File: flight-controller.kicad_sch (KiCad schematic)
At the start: 50 parts, among them J1 USB_C_Receptacle_USB2.0_16P, J2 Conn_Coaxial, J4 TC2030, SW1 SW_Push, U1 MIC5365-3.3YD5, U2 USBLC6-2SC6, U3 DLF162500LT-5028A1, U4 STM32WB55CEUx, U5 MPU-6050, X1 32kHz768, X2 32MHz

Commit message: BOM updates, minor routing improvements
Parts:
- C1, C14, C2, C3, C6: Distributor Link https://www.mouser.com/ProductDetail/KYOCERA-AVX/0603ZD475M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 -> https://www.digikey.com/en/products/detail/kyocera-avx/0402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
- C10, C11, C12, C13, C19, C20, C22, C4, C5, C7, C8, C9: Distributor Link https://www.mouser.com/ProductDetail/KYOCERA-AVX/0402X7R104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 -> https://www.digikey.com/en/products/detail/kyocera-avx/KGM0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; Manufacturer Part # 0402X7R104KT7AT -> KGM05AR51A104KH
- C15: Distributor Link (none) -> https://www.digikey.com/en/products/detail/kyocera-avx/0402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; Manufacturer (none) -> Kyocera AVX; Manufacturer Part # (none) -> 04025U0R8BAT2A
- C17, C18: Manufacturer (none) -> NOTE: Should make of type C0G
- X2: Distributor Link (none) -> https://www.digikey.com/en/products/detail/ndk-america-inc/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
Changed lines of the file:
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@@
 			)
 		)
-		(property "Distributor Link" "https://www.mouser.com/ProductDetail/KYOCERA-AVX/0402X7R104KT7AT?qs=sGAEpiMZZMukHu%252BjC5l7YTEDUe5eStCUp1B9Y37Xni8%3D"
+		(property "Distributor Link" "https://www.digikey.com/en/products/detail/kyocera-avx/KGM05AR51A104KH/563239"
 			(at 92.71 43.18 0)
 			(effects
@@
 			)
 		)
-		(property "Manufacturer Part #" "0402X7R104KT7AT"
+		(property "Manufacturer Part #" "KGM05AR51A104KH"
 			(at 92.71 43.18 0)
 			(effects
@@
 			)
 		)
-		(property "Manufacturer" ""
+		(property "Manufacturer" "NOTE: Should make of type C0G"
 			(at 166.37 110.49 0)
 			(effects
@@
 			)
 		)
-		(property "Distributor Link" "https://www.mouser.com/ProductDetail/KYOCERA-AVX/0402X7R104KT7AT?qs=sGAEpiMZZMukHu%252BjC5l7YTEDUe5eStCUp1B9Y37Xni8%3D"
+		(property "Distributor Link" "https://www.digikey.com/en/products/detail/kyocera-avx/KGM05AR51A104KH/563239"
 			(at 101.6 170.18 0)
 			(effects
@@
 			)
 		)
-		(property "Manufacturer Part #" "0402X7R104KT7AT"
+		(property "Manufacturer Part #" "KGM05AR51A104KH"
 			(at 101.6 170.18 0)
 			(effects
@@
 			)
 		)
-		(property "Distributor Link" "https://www.mouser.com/ProductDetail/KYOCERA-AVX/0603ZD475MAT2A?qs=sGAEpiMZZMsh%252B1woXyUXj3kzDK1MKLImRlrG%252BuVm%252Bt8%3D"
+		(property "Distributor Link" "https://www.digikey.com/en/products/detail/kyocera-avx/0402ZD475MAT2A/3080850"
 			(at 41.91 43.18 0)
 			(effects
@@
 			)
 		)
-		(property "Distributor Link" ""
+		(property "Distributor Link" "https://www.digikey.com/en/products/detail/kyocera-avx/04025U0R8BAT2A/2136276"
 			(at 201.93 86.36 0)
 			(effects
@@
 			)
 		)
-		(property "Manufacturer" ""
+		(property "Manufacturer" "Kyocera AVX"
 			(at 201.93 86.36 0)
 			(effects
@@
 			)
 		)
-		(property "Manufacturer Part #" ""
+		(property "Manufacturer Part #" "04025U0R8BAT2A"
 			(at 201.93 86.36 0)
 			(effects
@@
 			)
 		)
-		(property "Distributor Link" "https://www.mouser.com/ProductDetail/KYOCERA-AVX/0402X7R104KT7AT?qs=sGAEpiMZZMukHu%252BjC5l7YTEDUe5eStCUp1B9Y37Xni8%3D"
+		(property "Distributor Link" "https://www.digikey.com/en/products/detail/kyocera-avx/KGM05AR51A104KH/563239"
 			(at 139.7 27.94 0)
 			(effects
@@
 			)
 		)
-		(property "Manufacturer Part #" "0402X7R104KT7AT"
+		(property "Manufacturer Part #" "KGM05AR51A104KH"
 			(at 139.7 27.94 0)
 			(effects
@@
 			)
 		)
-		(property "Distributor Link" "https://www.mouser.com/ProductDetail/KYOCERA-AVX/0603ZD475MAT2A?qs=sGAEpiMZZMsh%252B1woXyUXj3kzDK1MKLImRlrG%252BuVm%252Bt8%3D"
+		(property "Distributor Link" "https://www.digikey.com/en/products/detail/kyocera-avx/0402ZD475MAT2A/3080850"
 			(at 87.63 26.67 0)
 			(effects
@@
 			)
 		)
-		(property "Distributor Link" "https://www.mouser.com/ProductDetail/KYOCERA-AVX/0603ZD475MAT2A?qs=sGAEpiMZZMsh%252B1woXyUXj3kzDK1MKLImRlrG%252BuVm%252Bt8%3D"
+		(property "Distributor Link" "https://www.digikey.com/en/products/detail/kyocera-avx/0402ZD475MAT2A/3080850"
 			(at 49.53 25.4 0)
 			(effects
@@
 			)
 		)
-		(property "Distributor Link" "https://www.mouser.com/ProductDetail/KYOCERA-AVX/0402X7R104KT7AT?qs=sGAEpiMZZMukHu%252BjC5l7YTEDUe5eStCUp1B9Y37Xni8%3D"
+		(property "Distributor Link" "https://www.digikey.com/en/products/detail/kyocera-avx/KGM05AR51A104KH/563239"
 			(at 105.41 43.18 0)
 			(effects
@@
 			)
 		)
-		(property "Manufacturer Part #" "0402X7R104KT7AT"
+		(property "Manufacturer Part #" "KGM05AR51A104KH"
 			(at 105.41 43.18 0)
 			(effects
@@
 			)
 		)
-		(property "Distributor Link" "https://www.mouser.com/ProductDetail/KYOCERA-AVX/0402X7R104KT7AT?qs=sGAEpiMZZMukHu%252BjC5l7YTEDUe5eStCUp1B9Y37Xni8%3D"
+		(property "Distributor Link" "https://www.digikey.com/en/products/detail/kyocera-avx/KGM05AR51A104KH/563239"
 			(at 121.92 26.67 0)
 			(effects
@@
 			)
 		)
-		(property "Manufacturer Part #" "0402X7R104KT7AT"
+		(property "Manufacturer Part #" "KGM05AR51A104KH"
 			(at 121.92 26.67 0)
 			(effects
@@
 			)
 		)
-		(property "Distributor Link" "https://www.mouser.com/ProductDetail/KYOCERA-AVX/0402X7R104KT7AT?qs=sGAEpiMZZMukHu%252BjC5l7YTEDUe5eStCUp1B9Y37Xni8%3D"
+		(property "Distributor Link" "https://www.digikey.com/en/products/detail/kyocera-avx/KGM05AR51A104KH/563239"
 			(at 210.82 115.57 0)
 			(effects
@@
 			)
 		)
-		(property "Manufacturer Part #" "0402X7R104KT7AT"
+		(property "Manufacturer Part #" "KGM05AR51A104KH"
 			(at 210.82 115.57 0)
 			(effects
@@
 			)
 		)
-		(property "Distributor Link" "https://www.mouser.com/ProductDetail/KYOCERA-AVX/0402X7R104KT7AT?qs=sGAEpiMZZMukHu%252BjC5l7YTEDUe5eStCUp1B9Y37Xni8%3D"
+		(property "Distributor Link" "https://www.digikey.com/en/products/detail/kyocera-avx/KGM05AR51A104KH/563239"
 			(at 80.01 43.18 0)
 			(effects
@@
 			)
 		)
-		(property "Manufacturer Part #" "0402X7R104KT7AT"
+		(property "Manufacturer Part #" "KGM05AR51A104KH"
 			(at 80.01 43.18 0)
 			(effects
@@
 			)
 		)
-		(property "Distributor Link" "https://www.mouser.com/ProductDetail/KYOCERA-AVX/0603ZD475MAT2A?qs=sGAEpiMZZMsh%252B1woXyUXj3kzDK1MKLImRlrG%252BuVm%252Bt8%3D"
+		(property "Distributor Link" "https://www.digikey.com/en/products/detail/kyocera-avx/0402ZD475MAT2A/3080850"
 			(at 109.22 26.67 0)
 			(effects
@@
 			)
 		)
-		(property "Distributor Link" "https://www.mouser.com/ProductDetail/KYOCERA-AVX/0402X7R104KT7AT?qs=sGAEpiMZZMukHu%252BjC5l7YTEDUe5eStCUp1B9Y37Xni8%3D"
+		(property "Distributor Link" "https://www.digikey.com/en/products/detail/kyocera-avx/KGM05AR51A104KH/563239"
 			(at 190.5 49.53 0)
 			(effects
@@
 			)
 		)
-		(property "Manufacturer Part #" "0402X7R104KT7AT"
+		(property "Manufacturer Part #" "KGM05AR51A104KH"
 			(at 190.5 49.53 0)
 			(effects
@@
 			)
 		)
-		(property "Distributor Link" ""
+		(property "Distributor Link" "https://www.digikey.com/en/products/detail/ndk-america-inc/CS06465-32M/7645290"
 			(at 193.04 100.33 0)
 			(effects
@@
 			)
 		)
-		(property "Distributor Link" "https://www.mouser.com/ProductDetail/KYOCERA-AVX/0402X7R104KT7AT?qs=sGAEpiMZZMukHu%252BjC5l7YTEDUe5eStCUp1B9Y37Xni8%3D"
+		(property "Distributor Link" "https://www.digikey.com/en/products/detail/kyocera-avx/KGM05AR51A104KH/563239"
 			(at 54.61 43.18 0)
 			(effects
@@
 			)
 		)
-		(property "Manufacturer Part #" "0402X7R104KT7AT"
+		(property "Manufacturer Part #" "KGM05AR51A104KH"
 			(at 54.61 43.18 0)
 			(effects
@@
 			)
 		)
-		(property "Distributor Link" "https://www.mouser.com/ProductDetail/KYOCERA-AVX/0402X7R104KT7AT?qs=sGAEpiMZZMukHu%252BjC5l7YTEDUe5eStCUp1B9Y37Xni8%3D"
+		(property "Distributor Link" "https://www.digikey.com/en/products/detail/kyocera-avx/KGM05AR51A104KH/563239"
 			(at 118.11 43.18 0)
 			(effects
@@
 			)
 		)
-		(property "Manufacturer Part #" "0402X7R104KT7AT"
+		(property "Manufacturer Part #" "KGM05AR51A104KH"
 			(at 118.11 43.18 0)
 			(effects
@@
 			)
 		)
-		(property "Distributor Link" "https://www.mouser.com/ProductDetail/KYOCERA-AVX/0402X7R104KT7AT?qs=sGAEpiMZZMukHu%252BjC5l7YTEDUe5eStCUp1B9Y37Xni8%3D"
+		(property "Distributor Link" "https://www.digikey.com/en/products/detail/kyocera-avx/KGM05AR51A104KH/563239"
 			(at 64.77 184.15 0)
 			(effects
@@
 			)
 		)
-		(property "Manufacturer Part #" "0402X7R104KT7AT"
+		(property "Manufacturer Part #" "KGM05AR51A104KH"
 			(at 64.77 184.15 0)
 			(effects
@@
 			)
 		)
-		(property "Manufacturer" ""
+		(property "Manufacturer" "NOTE: Should make of type C0G"
 			(at 176.53 110.49 0)
 			(effects
@@
 			)
 		)
-		(property "Distributor Link" "https://www.mouser.com/ProductDetail/KYOCERA-AVX/0402X7R104KT7AT?qs=sGAEpiMZZMukHu%252BjC5l7YTEDUe5eStCUp1B9Y37Xni8%3D"
+		(property "Distributor Link" "https://www.digikey.com/en/products/detail/kyocera-avx/KGM05AR51A104KH/563239"
 			(at 67.31 43.18 0)
 			(effects
@@
 			)
 		)
-		(property "Manufacturer Part #" "0402X7R104KT7AT"
+		(property "Manufacturer Part #" "KGM05AR51A104KH"
 			(at 67.31 43.18 0)
 			(effects
@@
 			)
 		)
-		(property "Distributor Link" "https://www.mouser.com/ProductDetail/KYOCERA-AVX/0603ZD475MAT2A?qs=sGAEpiMZZMsh%252B1woXyUXj3kzDK1MKLImRlrG%252BuVm%252Bt8%3D"
+		(property "Distributor Link" "https://www.digikey.com/en/products/detail/kyocera-avx/0402ZD475MAT2A/3080850"
 			(at 190.5 66.04 0)
 			(effects

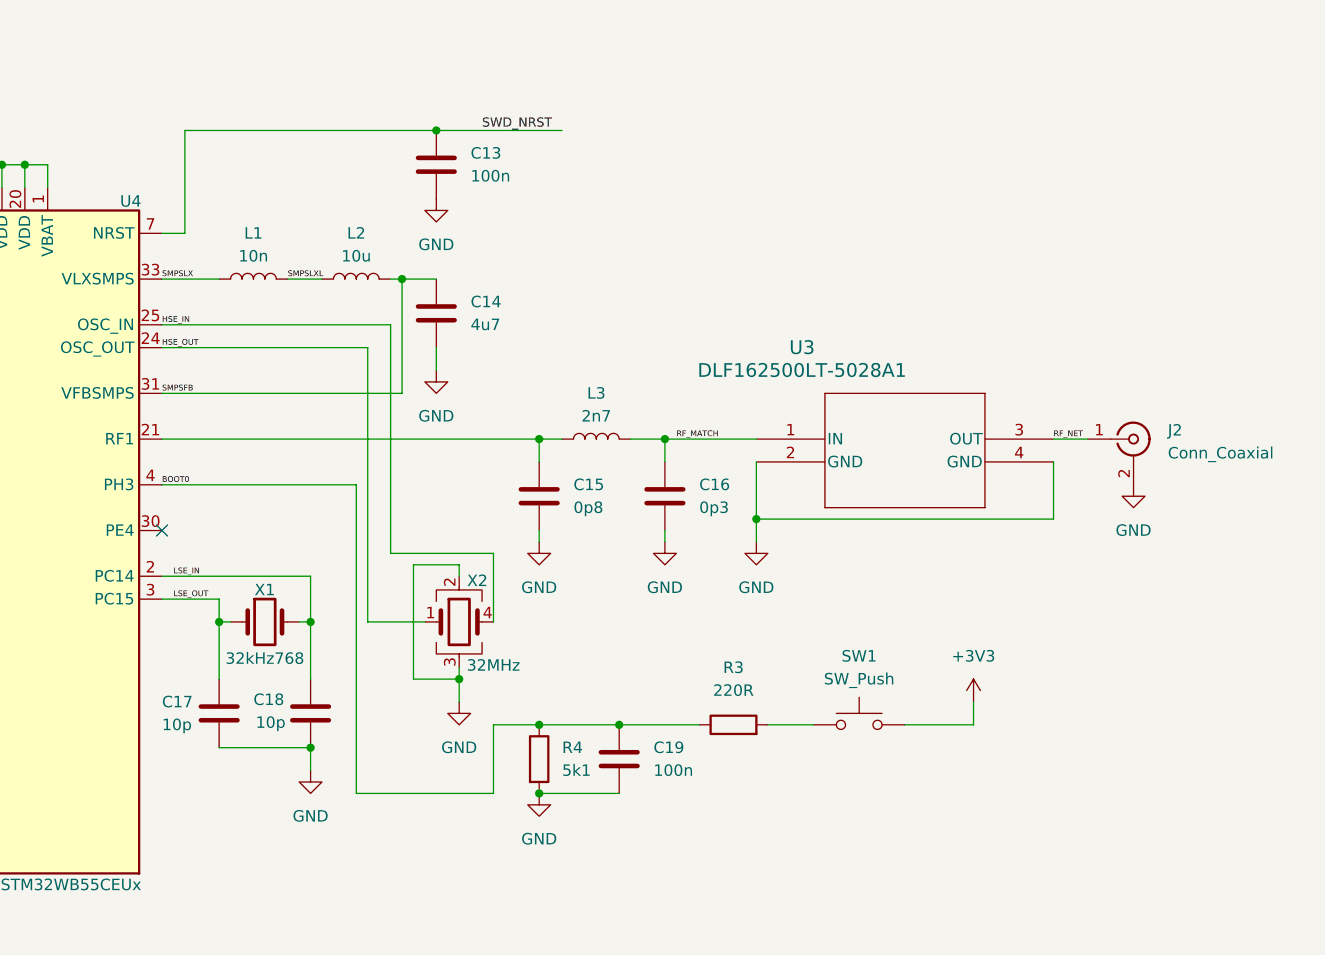
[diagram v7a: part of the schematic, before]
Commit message: BOM done, footprints & layout updated.
Layout for both crystal oscillators revised.
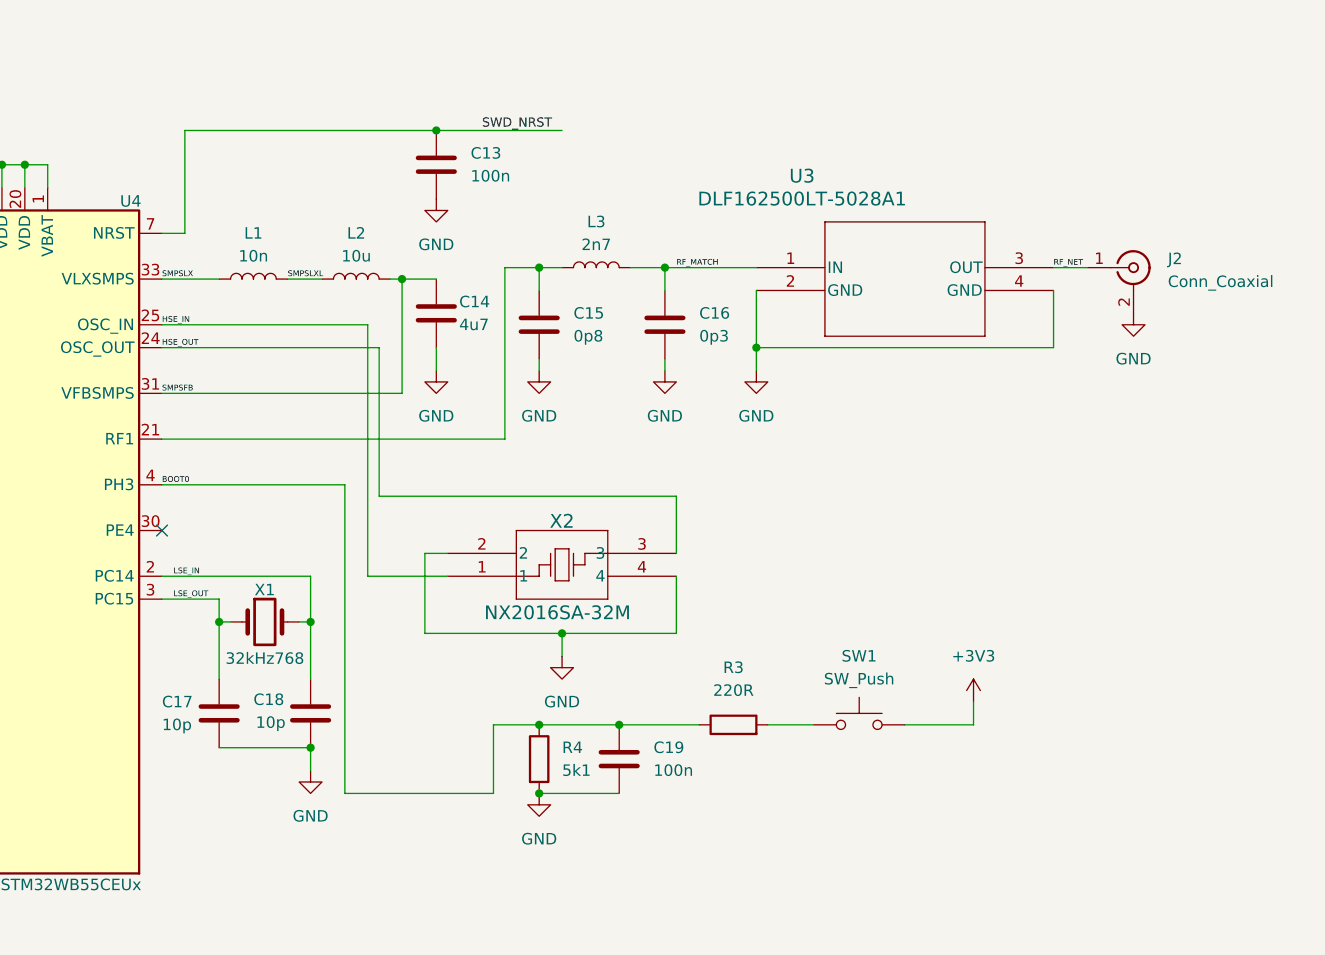
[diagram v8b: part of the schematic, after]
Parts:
- removed X2: 32MHz, Crystal:Crystal_SMD_2016-4Pin_2.0x1.6mm, symbol Device:Crystal_GND23
- added X2: NX2016SA-32M, Library:NX2016SA_NDK, symbol Library:NX2016SA-32M-EXS00A-CS06465
- C16: Distributor Link (none) -> https://www.digikey.com/en/products/detail/murata-electroni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; Manufacturer (none) -> Murata; Manufacturer Part # (none) -> GRM1555C1HR30BA01J
- C17, C18: Distributor Link (none) -> https://www.digikey.com/en/products/detail/murata-electroni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; Manufacturer NOTE: Should make of type C0G -> Murata; Manufacturer Part # (none) -> GRM1555C1H100JA01D
- C21: Distributor Link (none) -> https://www.digikey.com/en/products/detail/murata-electroni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; Manufacturer (none) -> Murata; Manufacturer Part # (none) -> GRM155R71C103KA01D
- C23: Distributor Link (none) -> https://www.digikey.com/en/products/detail/murata-electroni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; Manufacturer (none) -> Murata; Manufacturer Part # (none) -> GRM155R61C222KA01D
- J1: Distributor Link (none) -> https://www.digikey.com/en/products/detail/gct/USB4105-GF-A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; Manufacturer (none) -> GCT; Manufacturer Part # (none) -> USB4105-GF-A
- J2: Distributor Link (none) -> https://www.digikey.com/en/products/detail/hirose-electric-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; Manufacturer (none) -> Hirose; Manufacturer Part # (none) -> U.FL-R-SMT-1(01)
- L1: Distributor Link (none) -> https://www.digikey.com/en/products/detail/murata-electroni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; Manufacturer (none) -> Murata; Manufacturer Part # (none) -> LQG15WZ10NJ02D
- L2: Distributor Link (none) -> https://www.digikey.com/en/products/detail/murata-electroni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; Manufacturer (none) -> Murata; Manufacturer Part # (none) -> LQM21FN100m70L
- L3: Distributor Link (none) -> https://www.digikey.com/en/products/detail/murata-electroni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; Manufacturer (none) -> Murata; Manufacturer Part # (none) -> LQG15HS2N7S02
- R1, R2, R4: Distributor Link (none) -> https://www.digikey.com/en/products/detail/panasonic-electr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; Manufacturer (none) -> Panasonic; Manufacturer Part # (none) -> ERJ-2GEJ512X
- R3: Distributor Link (none) -> https://www.digikey.com/en/products/detail/yageo/RC0402JR-0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; Manufacturer (none) -> Yageo; Manufacturer Part # (none) -> RC0402JR-07220RL
- R5, R6: Distributor Link (none) -> https://www.digikey.com/en/products/detail/panasonic-electr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; Manufacturer (none) -> Panasonic; Manufacturer Part # (none) -> ERJ-2RKF2201X
- SW1: Distributor Link (none) -> https://www.digikey.com/en/products/detail/c-k/RS-282G05A3-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; Manufacturer (none) -> C&K; Manufacturer Part # (none) -> RS-282G05A3-SM RT
- U1: Distributor Link (none) -> https://www.digikey.com/en/products/detail/microchip-techno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; Manufacturer (none) -> Microchip Technology; Manufacturer Part # (none) -> MIC5365-3.3YD5-TR
- U2: Distributor Link (none) -> https://www.digikey.com/en/products/detail/stmicroelectroni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; Manufacturer (none) -> STMicroelectronics; Manufacturer Part # (none) -> USBLC6-2SC6
- U3: Distributor Link (none) -> https://www.digikey.com/en/products/detail/tdk-corporation/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; Manufacturer (none) -> TDK; Manufacturer Part # (none) -> DLF162500LT-5028A1
- U4: Distributor Link (none) -> https://www.digikey.com/en/products/detail/stmicroelectroni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; Manufacturer (none) -> STMicroelectronics; Manufacturer Part # (none) -> STM32WB55CEU6
- U5: Distributor Link (none) -> https://www.digikey.com/en/products/detail/tdk-invensense/M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; Manufacturer (none) -> TDK InvenSense; Manufacturer Part # (none) -> MPU-6050
- X1: footprint Crystal:Crystal_SMD_2012-2Pin_2.0x1.2mm -> Library:XTAL_NX2012SA_NDK; Distributor Link (none) -> https://www.digikey.com/en/products/detail/ndk-america-inc/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; Manufacturer (none) -> NDK; Manufacturer Part # (none) -> STDMUB1-32.768K
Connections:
- net GND: now also X2.2, X2.4
- net HSE_IN: now also X2.1
- net HSE_OUT: now also X2.3
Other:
- moved on the sheet: C15, C16, J2, L3, U3
